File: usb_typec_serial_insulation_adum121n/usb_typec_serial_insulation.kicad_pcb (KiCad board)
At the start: 2 copper layers, 20 x 17 mm, 3 parts, among them J1 Conn_01x06_Socket, J2 Conn_01x06_Socket, U1 ADuM121N

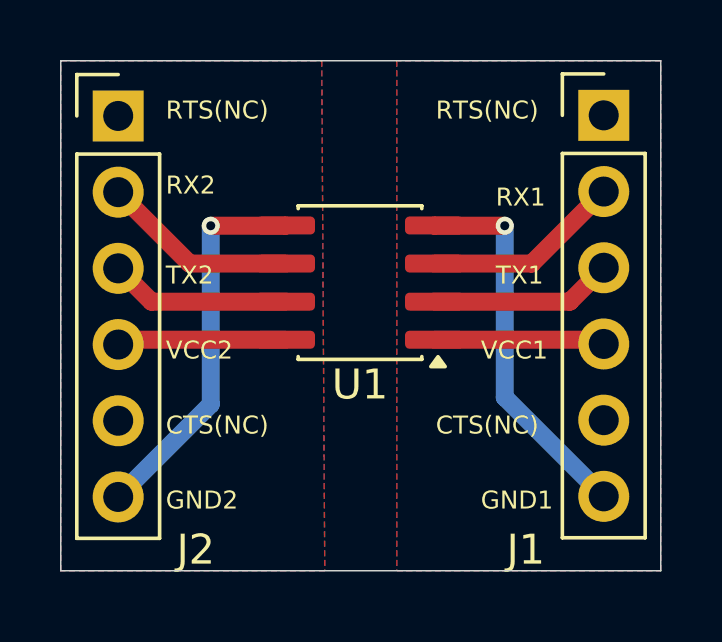
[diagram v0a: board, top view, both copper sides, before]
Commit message: add C1, C2 adum121N V1.1
add C1, C2 adum121N V1.1
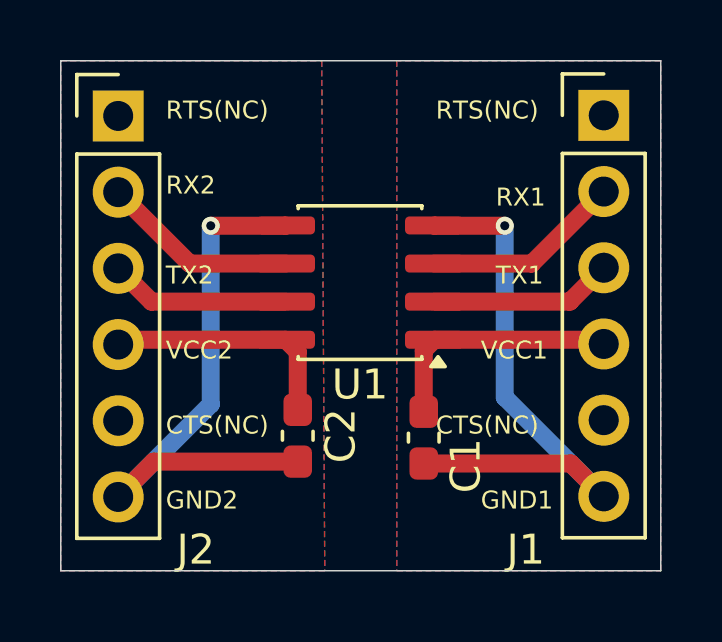
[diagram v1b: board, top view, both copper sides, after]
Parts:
- added C1: 0.1uF,10V(=5V*2), Capacitor_SMD:C_0603_1608Metric_Pad1.08x0.95mm_HandSolder, F.Cu at (140.1, 101.6)
- added C2: 0.1uF,10V(=5V*2), Capacitor_SMD:C_0603_1608Metric_Pad1.08x0.95mm_HandSolder, F.Cu at (135.9, 101.5)
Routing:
- net GND2: track 12.8 -> 19.3 mm
- net GND1: track 12.7 -> 19.2 mm
- net VCC1: track 5.71 -> 8.25 mm
- net VCC2: track 5.65 -> 8.15 mm
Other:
- board text added: "usb typec serial inslation ADuM121N V1.1 260212 takurx"
- board text removed: "usb typec serial inslation ADuM121N V1.0 260211 takurx"

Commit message: modify 121N, V2.0
modify 121N, V2.0
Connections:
- U1 pad 2: Net-(J1-Pin_3) -> Net-(J1-Pin_2)
- U1 pad 3: Net-(J1-Pin_2) -> Net-(J1-Pin_3)
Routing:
- net Net-(J1-Pin_2): track 6.64 -> 8.63 mm, vias 0 -> 2
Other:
- board text added: "-> VIA TXD"
- board text added: "-> VOA RXD"
- board text added: "<- VIB TXD"
- board text added: "<- VOB RXD"
- board text added: "NC"
- board text added: "usb typec serial inslation ADuM121N V2.0 260326 takurx"
- board text removed: "CTS(NC)"
- board text removed: "RTS(NC)"
- board text removed: "RX1"
- board text removed: "RX2"
- board text removed: "TX1"
- board text removed: "TX2"
- board text removed: "usb typec serial inslation ADuM121N V1.1 260212 takurx"
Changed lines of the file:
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@@
 	(title_block
 		(title "usb typec serial insulation")
-		(date "2026-02-12")
-		(rev "V1.1")
+		(date "2026-03-26")
+		(rev "V2.0")
 		(company "takurx")
 		(comment 1 "ADuM121N")
 		(comment 2 "add C1, C2")
+		(comment 3 "modify pinout 2, 3")
 	)
 	(layers
@@
 			(layers "F.Cu" "F.Mask" "F.Paste")
 			(roundrect_rratio 0.25)
-			(net 2 "Net-(J1-Pin_3)")
+			(net 3 "Net-(J1-Pin_2)")
 			(pinfunction "VOA")
 			(pintype "output")
@@
 			(layers "F.Cu" "F.Mask" "F.Paste")
 			(roundrect_rratio 0.25)
-			(net 3 "Net-(J1-Pin_2)")
+			(net 2 "Net-(J1-Pin_3)")
 			(pinfunction "VIB")
 			(pintype "input")
@@
 	)
 	(gr_text "GND2"
-		(at 131.5 104 0)
+		(at 131.75 103.95 0)
 		(layer "F.SilkS")
 		(effects
@@
 		)
 	)
-	(gr_text "RX2"
-		(at 131.5 93.5 0)
+	(gr_text "<-\nVOB\nRXD"
+		(at 131.95 94.5 0)
 		(layer "F.SilkS")
 		(effects
@@
 		)
 	)
-	(gr_text "TX2"
-		(at 131.5 96.5 0)
+	(gr_text "->\nVIA\nTXD"
+		(at 132 97.4 0)
 		(layer "F.SilkS")
 		(effects
@@
 	)
 	(gr_text "GND1"
-		(at 142 104 0)
+		(at 141.75 104.15 0)
 		(layer "F.SilkS")
 		(effects
@@
 		)
 	)
-	(gr_text "TX1"
-		(at 142.5 96.5 0)
+	(gr_text "<-\nVIB\nTXD"
+		(at 142.45 97.6 0)
 		(layer "F.SilkS")
 		(effects
@@
 		)
 	)
-	(gr_text "RTS(NC)"
-		(at 131.5 91 0)
+	(gr_text "NC"
+		(at 131.8 91.25 0)
 		(layer "F.SilkS")
 		(effects
@@
 		)
 	)
-	(gr_text "RX1"
-		(at 142.5 93.9 0)
+	(gr_text "->\nVOA\nRXD"
+		(at 142.4 94.5 0)
 		(layer "F.SilkS")
 		(effects
@@
 		)
 	)
-	(gr_text "CTS(NC)"
-		(at 131.5 101.5 0)
+	(gr_text "NC"
+		(at 131.85 101.5 0)
 		(layer "F.SilkS")
 		(effects
@@
 		)
 	)
-	(gr_text "RTS(NC)"
-		(at 140.5 91 0)
+	(gr_text "NC"
+		(at 142.55 91.15 0)
 		(layer "F.SilkS")
 		(effects
@@
 		)
 	)
-	(gr_text "CTS(NC)"
-		(at 140.5 101.5 0)
+	(gr_text "NC"
+		(at 142.6 101.5 0)
 		(layer "F.SilkS")
 		(effects
@@
 		)
 	)
-	(gr_text "usb typec serial inslation\nADuM121N\nV1.1 260212 takurx"
+	(gr_text "usb typec serial inslation\nADuM121N\nV2.0 260326 takurx"
 		(at 144 89.7 90)
 		(layer "B.SilkS")
@@
 	)
 	(segment
-		(start 140.45 97.03)
-		(end 144.97 97.03)
+		(start 140.59 95.9)
+		(end 140.45 95.76)
 		(width 0.6)
 		(layer "F.Cu")
@@
 	)
 	(segment
-		(start 144.97 97.03)
-		(end 146.1 95.9)
+		(start 146.1 95.9)
+		(end 140.59 95.9)
 		(width 0.6)
 		(layer "F.Cu")
@@
 	)
 	(segment
-		(start 143.7 95.76)
-		(end 146.1 93.36)
+		(start 143.9 97)
+		(end 140.48 97)
 		(width 0.6)
 		(layer "F.Cu")
@@
 	)
 	(segment
-		(start 140.45 95.76)
-		(end 143.7 95.76)
-		(width 0.6)
-		(layer "F.Cu")
+		(start 140.48 97)
+		(end 140.45 97.03)
+		(width 0.6)
+		(layer "F.Cu")
+		(net 3)
+	)
+	(segment
+		(start 145.04 93.36)
+		(end 143.9 94.5)
+		(width 0.6)
+		(layer "F.Cu")
+		(net 3)
+	)
+	(segment
+		(start 146.1 93.36)
+		(end 145.04 93.36)
+		(width 0.6)
+		(layer "F.Cu")
+		(net 3)
+	)
+	(via
+		(at 143.9 94.5)
+		(size 0.6)
+		(drill 0.3)
+		(layers "F.Cu" "B.Cu")
+		(net 3)
+	)
+	(via
+		(at 143.9 97)
+		(size 0.6)
+		(drill 0.3)
+		(layers "F.Cu" "B.Cu")
+		(net 3)
+	)
+	(segment
+		(start 143.9 94.5)
+		(end 143.9 97)
+		(width 0.6)
+		(layer "B.Cu")
 		(net 3)
 	)
@@
 	)
 	(segment
-		(start 142.8 100.22)
-		(end 142.8 94.5)
+		(start 142.8 94.5)
+		(end 142.8 100.22)
 		(width 0.6)
 		(layer "B.Cu")

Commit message: add pinout description
add pinout description
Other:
- board text added: "-> VIB TXD"
- board text added: "-> VOB RXD"
- board text added: "<- VIA TXD"
- board text added: "<- VOA RXD"
- board text added: "usb typec serial inslation ADuM121N V2.1 260430 takurx"
- board text removed: "usb typec serial inslation ADuM121N V2.0 260326 takurx"
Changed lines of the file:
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@@
 	(title_block
 		(title "usb typec serial insulation")
-		(date "2026-03-26")
-		(rev "V2.0")
+		(date "2026-04-30")
+		(rev "V2.1")
 		(company "takurx")
 		(comment 1 "ADuM121N")
 		(comment 2 "add C1, C2")
 		(comment 3 "modify pinout 2, 3")
+		(comment 4 "add pinout description")
 	)
 	(layers
@@
 		)
 	)
-	(gr_text "usb typec serial inslation\nADuM121N\nV2.0 260326 takurx"
-		(at 144 89.7 90)
+	(gr_text "NC"
+		(at 133.8 91.3 -0)
+		(layer "B.SilkS")
+		(effects
+			(font
+				(size 0.6 0.6)
+				(thickness 0.075)
+			)
+			(justify left bottom mirror)
+		)
+	)
+	(gr_text "NC"
+		(at 134.155 101.5 -0)
+		(layer "B.SilkS")
+		(effects
+			(font
+				(size 0.6 0.6)
+				(thickness 0.075)
+			)
+			(justify left bottom mirror)
+		)
+	)
+	(gr_text "->\nVIB\nTXD"
+		(at 143.6 97.6 0)
+		(layer "B.SilkS")
+		(effects
+			(font
+				(size 0.6 0.6)
+				(thickness 0.075)
+			)
+			(justify left bottom mirror)
+		)
+	)
+	(gr_text "GND1"
+		(at 144.140714 104.15 -0)
+		(layer "B.SilkS")
+		(effects
+			(font
+				(size 0.6 0.6)
+				(thickness 0.075)
+			)
+			(justify left bottom mirror)
+		)
+	)
+	(gr_text "NC"
+		(at 143.6 91.2 -0)
+		(layer "B.SilkS")
+		(effects
+			(font
+				(size 0.6 0.6)
+				(thickness 0.075)
+			)
+			(justify left bottom mirror)
+		)
+	)
+	(gr_text "<-\nVIA\nTXD"
+		(at 134.005 97.4 0)
+		(layer "B.SilkS")
+		(effects
+			(font
+				(size 0.6 0.6)
+				(thickness 0.075)
+			)
+			(justify left bottom mirror)
+		)
+	)
+	(gr_text "VCC2"
+		(at 134.1 99 -0)
+		(layer "B.SilkS")
+		(effects
+			(font
+				(size 0.6 0.6)
+				(thickness 0.075)
+			)
+			(justify left bottom mirror)
+		)
+	)
+	(gr_text "usb typec serial inslation\nADuM121N\nV2.1 260430 takurx"
+		(at 139.6 89.7 90)
 		(layer "B.SilkS")
 		(effects
@@
 			)
 			(justify left bottom mirror)
+		)
+	)
+	(gr_text "NC"
+		(at 143.290714 101.5 -0)
+		(layer "B.SilkS")
+		(effects
+			(font
+				(size 0.6 0.6)
+				(thickness 0.075)
+			)
+			(justify left bottom mirror)
+		)
+	)
+	(gr_text "->\nVOB\nRXD"
+		(at 134.055 94.5 0)
+		(layer "B.SilkS")
+		(effects
+			(font
+				(size 0.6 0.6)
+				(thickness 0.075)
+			)
+			(justify left bottom mirror)
+		)
+	)
+	(gr_text "VCC1"
+		(at 144.1 99 -0)
+		(layer "B.SilkS")
+		(effects
+			(font
+				(size 0.6 0.6)
+				(thickness 0.075)
+			)
+			(justify left bottom mirror)
+		)
+	)
+	(gr_text "<-\nVOA\nRXD"
+		(at 143.7 94.5 0)
+		(layer "B.SilkS")
+		(effects
+			(font
+				(size 0.6 0.6)
+				(thickness 0.075)
+			)
+			(justify left bottom mirror)
+		)
+	)
+	(gr_text "GND2"
+		(at 134.255 103.95 -0)
+		(layer "B.SilkS")
+		(effects
+			(font
+				(size 0.6 0.6)
+				(thickness 0.075)
+			)
+			(justify left bottom mirror)
